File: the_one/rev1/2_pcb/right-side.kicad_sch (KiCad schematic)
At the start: 39 parts, among them SW20 KeySwitch, SW21 KeySwitch, SW22 KeySwitch, SW23 KeySwitch, SW24 KeySwitch, SW25 KeySwitch, SW26 KeySwitch, SW27 KeySwitch, SW28 KeySwitch, SW29 KeySwitch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

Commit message: update KiCAD schematcis
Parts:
- U2: footprint RPi_Pico:RPi_Pico_SMD_TH -> MCU_RaspberryPi_and_Boards:RPi_Pico_SMD_TH
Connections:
- net E-INK_BUSY: now reaches U2.10 (GPIO7)
- net E-INK_RST: now reaches U2.11 (GPIO8)
- net E-INK_DC: now reaches U2.12 (GPIO9)
- net E-INK_VCC: now reaches U2.36 (3V3)
- net SPI1_CK renamed E-INK_SCK
- net SPI1_CS renamed E-INK_CS
- net SPI1_RX: no longer names the net of U2.16 (GPIO12)
- net SPI1_TX renamed E-INK_MOSI
- no-connect marks 18 -> 15
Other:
- moved on the sheet: U2

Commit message: update rev1 README
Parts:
- U2: value Pico -> RP2040
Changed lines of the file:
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@@
 			)
 		)
-		(property "Value" "Pico"
+		(property "Value" "RP2040"
 			(at 228.6 52.07 0)
 			(show_name no)

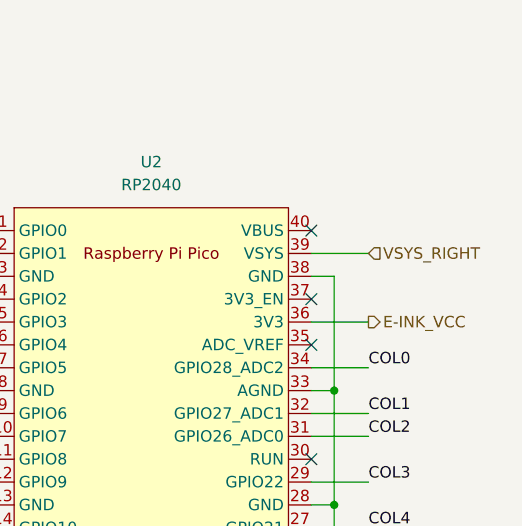
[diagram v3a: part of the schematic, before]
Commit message: change power supply pins of rp2040 from VSYS to VBUS
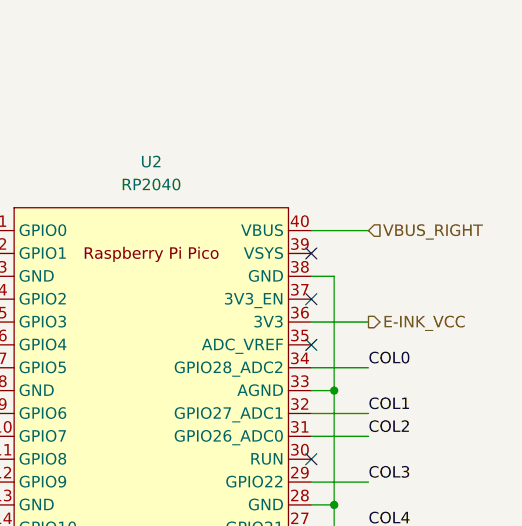
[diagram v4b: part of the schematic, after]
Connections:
- net VBUS_RIGHT: now reaches U2.40 (VBUS)
- net VSYS_RIGHT: no longer names the net of U2.39 (VSYS)
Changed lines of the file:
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@@
-	)
-	(no_connect
-		(at 246.38 57.15)
 	)
 	(no_connect
@@
 	)
 	(no_connect
+		(at 246.38 59.69)
+	)
+	(no_connect
 		(at 246.38 64.77)
 	)
@@
 	(wire
 		(pts
+			(xy 246.38 57.15) (xy 252.73 57.15)
+		)
+		(stroke
+			(width 0)
+			(type default)
+		)
+	)
+	(wire
+		(pts
 			(xy 80.01 39.37) (xy 80.01 52.07)
 		)
@@
 		(pts
 			(xy 59.69 52.07) (xy 59.69 83.82)
-		)
-		(stroke
-			(width 0)
-			(type default)
-		)
-	)
-	(wire
-		(pts
-			(xy 246.38 59.69) (xy 252.73 59.69)
 		)
 		(stroke
@@
 		)
 	)
-	(hierarchical_label "VSYS_RIGHT"
+	(hierarchical_label "VBUS_RIGHT"
 		(shape input)
-		(at 252.73 59.69 0)
-		(effects
-			(font
+		(at 252.73 57.15 0)
+		(effects
+			(font

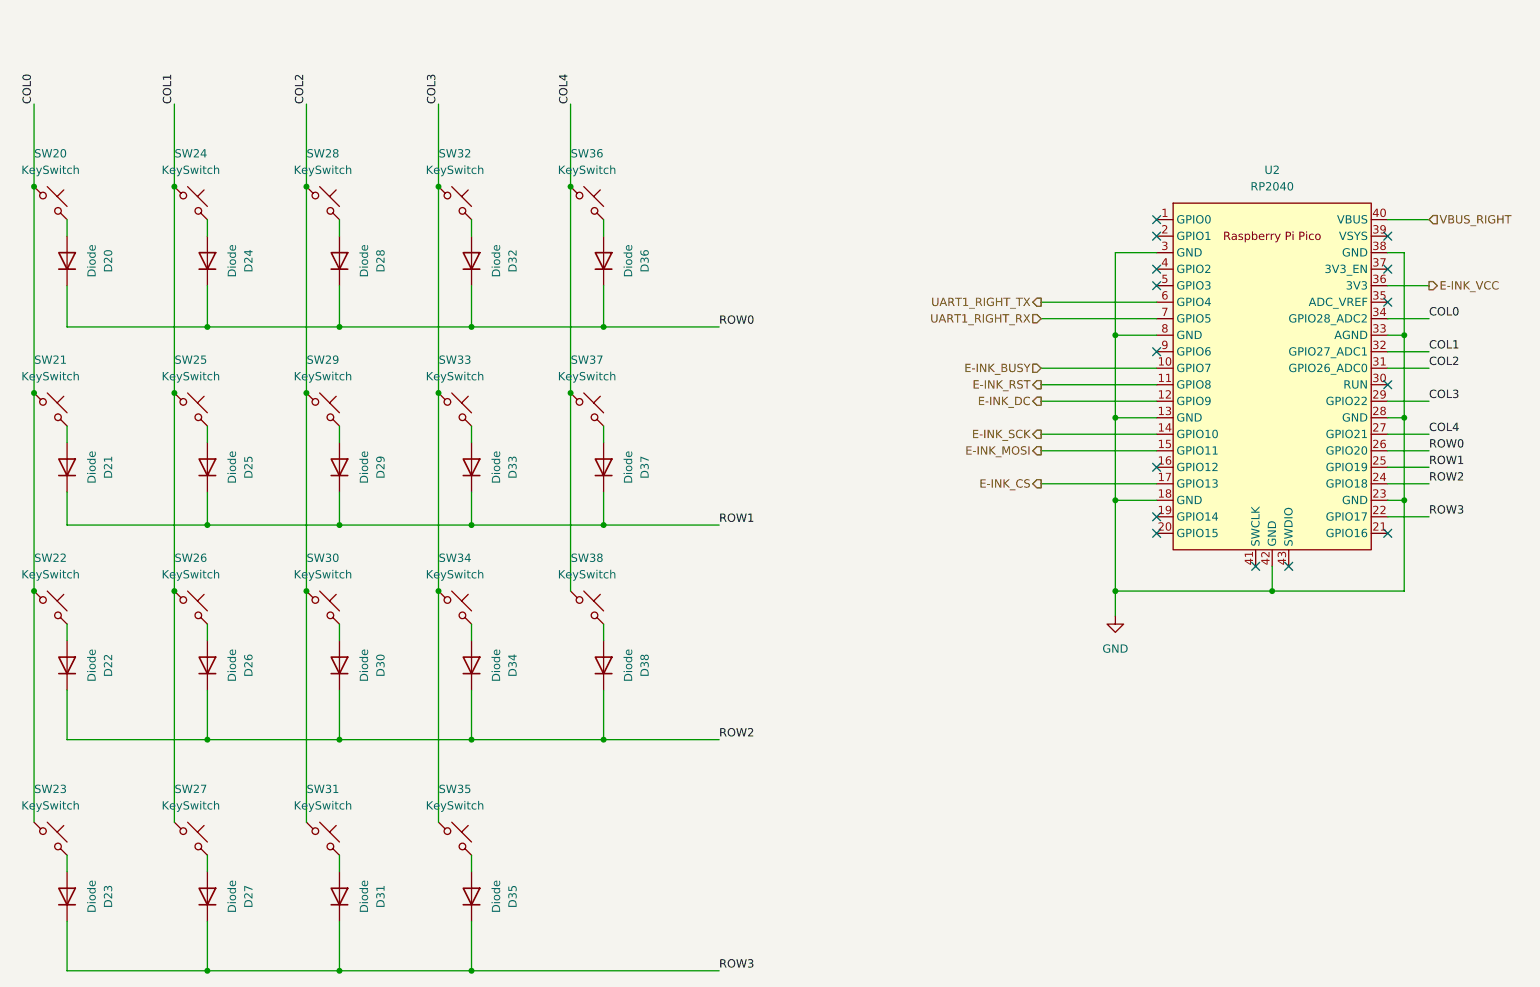
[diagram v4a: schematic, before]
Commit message: add TRRS jacks into the schematics
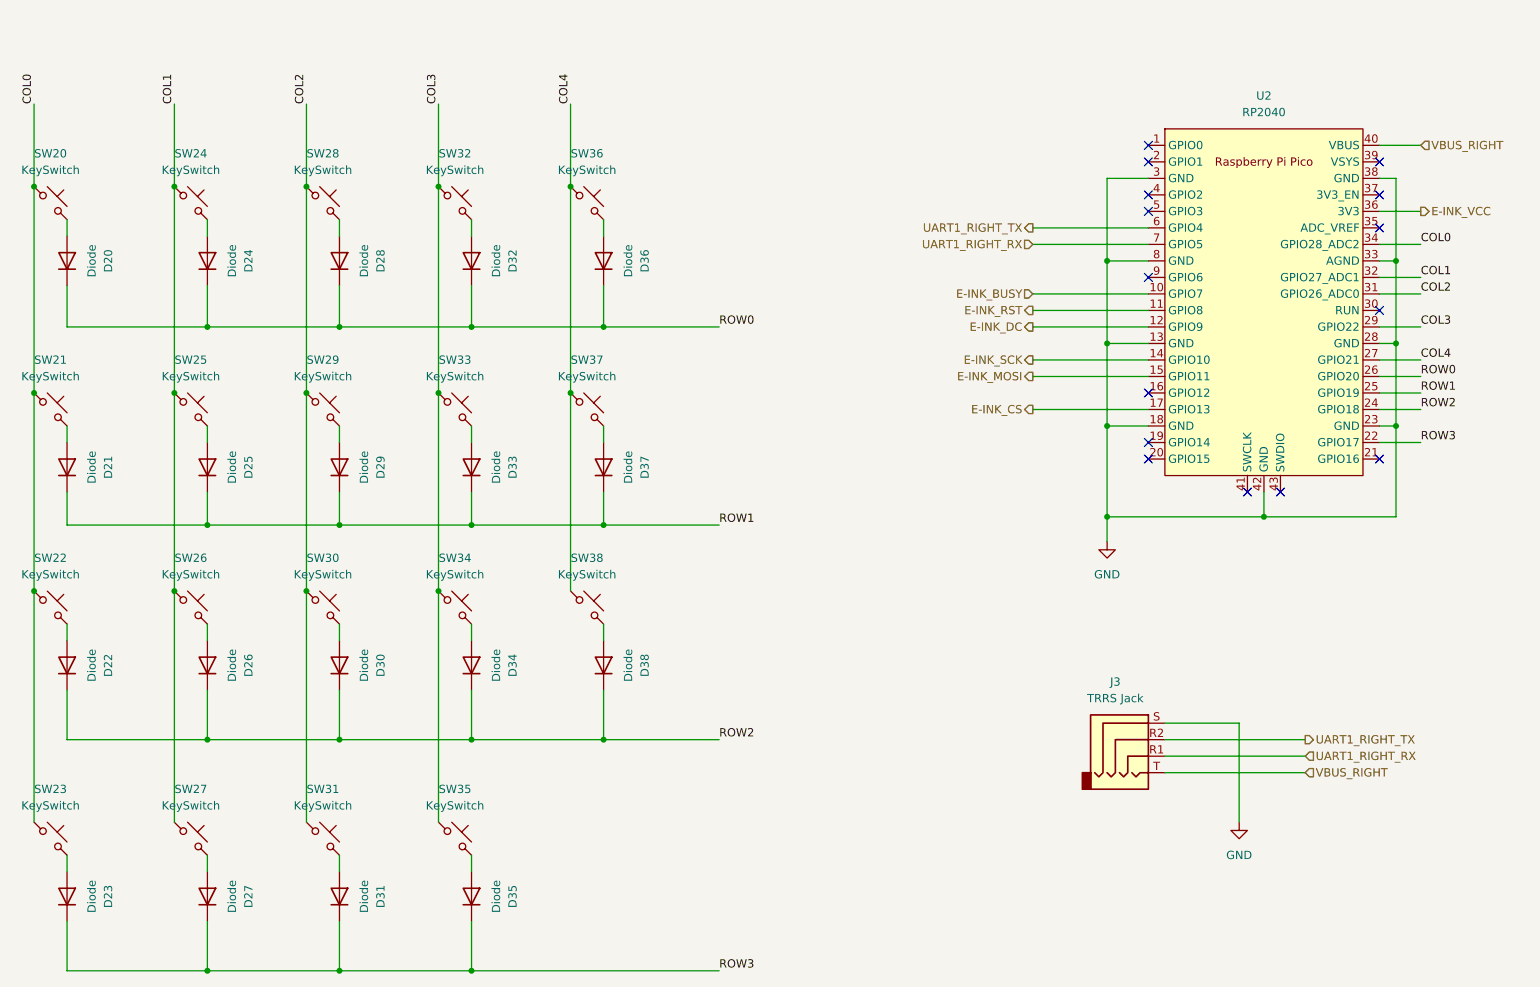
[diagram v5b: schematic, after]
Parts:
- added J3: TRRS Jack, symbol Connector_Audio:AudioJack4
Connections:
- net GND: now also J3.S
- net UART1_RIGHT_RX: now also J3.R1
- net UART1_RIGHT_TX: now also J3.R2
- net VBUS_RIGHT: now also J3.T
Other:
- moved on the sheet: U2
